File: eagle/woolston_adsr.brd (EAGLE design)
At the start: 100 x 80 mm, 39 parts, among them IC1 TL074P, Q1 2N3906, T1 2N3904

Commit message: almost layout
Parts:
- D2, D3: value 1N4148DO35-10 -> 1N4148DO35-7; device diode:DO35-10 -> diode:DO35-7
- moved R11 3.81 mm to (15.2, 22.9)
- moved R1 3.81 mm to (15.2, 19.1)
- moved R10 2.54 mm to (34.3, 20.3)
- moved R15 2.54 mm to (66.0, 22.9)
- moved D1 1.80 mm to (53.3, 11.4)
- moved D3 1.27 mm to (24.1, 15.2)
- moved R12 1.27 mm to (64.8, 14.0)
- moved R6 1.27 mm to (16.5, 41.9)
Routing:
- net N$4: track 69.7 -> 66.0 mm
- net GND: track 342.2 -> 339.4 mm
- net N$6: track 43.0 -> 45.8 mm
- net N$22: track 11.5 -> 14.1 mm
- net N$24: track 19.0 -> 16.7 mm
- net N$18: track 31.6 -> 33.5 mm
- net N$21: track 7.12 -> 5.24 mm
- net N$25: track 11.0 -> 9.20 mm
- net N$9: track 3.59 -> 4.58 mm
- net N$14: track 28.3 -> 29.3 mm
- net +12V: track 83.7 -> 84.6 mm

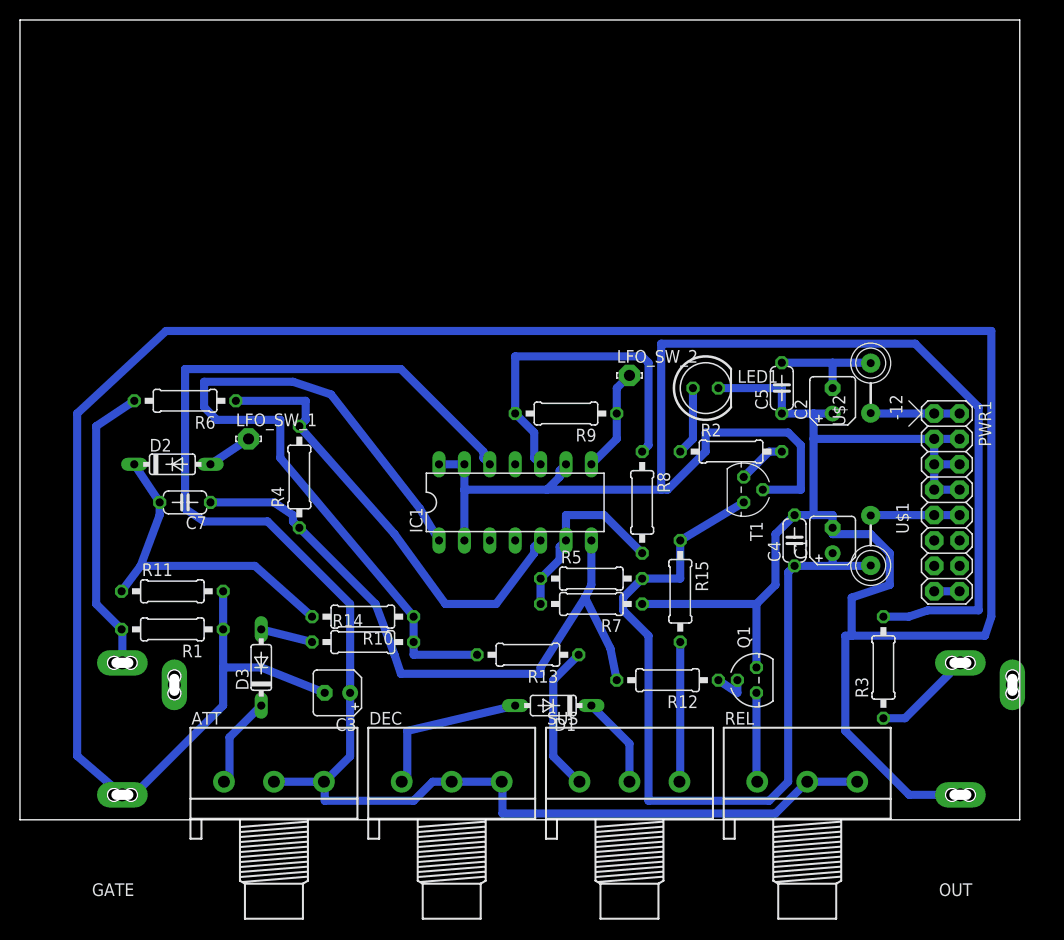
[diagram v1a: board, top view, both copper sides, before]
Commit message: fixed power to 074 and twiggled some
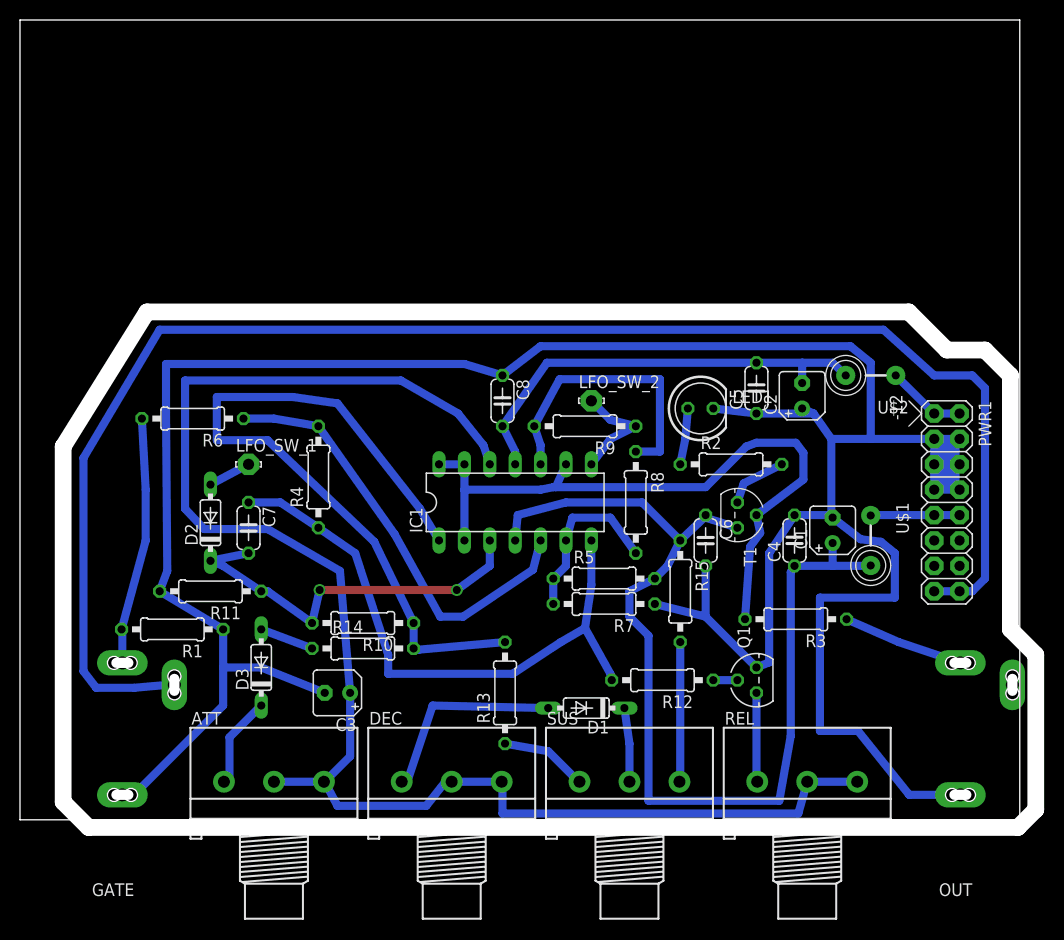
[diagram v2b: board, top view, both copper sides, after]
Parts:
- added C6, C8: 100n, rcl:C050-024X044
- moved R3 10.0 mm to (77.6, 20.1), turned to 180 degrees
- moved D2 6.97 mm to (19.1, 29.7), turned to 90 degrees
- moved C7 6.84 mm to (22.9, 29.2), turned to 270 degrees
- moved LFO_SW_2 4.58 mm to (57.1, 41.9)
- moved R13 4.44 mm to (48.5, 12.7), turned to 90 degrees
- moved R11 3.81 mm to (19.1, 22.9), turned to 180 degrees
- moved D1 3.31 mm to (56.6, 11.2)
- moved C2 3.09 mm to (78.2, 42.4)
- moved T1 2.62 mm to (71.8, 30.5)
- moved C5 2.54 mm to (73.7, 43.2)
- moved LFO_SW_1 2.54 mm to (22.9, 35.6)
- moved R9 2.29 mm to (56.5, 39.4)
- moved LED1 2.09 mm to (68.1, 41.1)
- moved R6 1.93 mm to (17.3, 40.1)
- moved R4 1.90 mm to (29.8, 34.3)
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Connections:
- removed net V+: IC1.4
- removed net V-: IC1.11
- net +12V: now also C6.1, IC1.4
- net -12V: now also C8.2, IC1.11
- net GND: now also C6.2, C8.1
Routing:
- net N$12: track 2.54 -> 155.7 mm
- net N$19: track 138.3 -> 68.2 mm
- net GND: track 339.4 -> 275.3 mm
- net -12V: track 11.5 -> 44.3 mm
- net +12V: track 84.6 -> 103.6 mm
- net N$18: track 33.5 -> 39.7 mm, vias 0 -> 2
- net N$16: track 14.9 -> 8.78 mm
- net N$10: track 34.6 -> 28.9 mm
- net N$4: track 66.0 -> 60.5 mm
- net N$14: track 29.3 -> 24.8 mm
- net N$24: track 16.7 -> 20.1 mm
- net N$20: track 76.5 -> 74.1 mm
- net N$15: track 9.99 -> 12.2 mm
- net N$6: track 45.8 -> 43.9 mm
- net N$25: track 9.20 -> 7.40 mm
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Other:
- board size 100 x 80 mm -> 101.6 x 80.8 mm

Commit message: verified and new panel
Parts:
- moved R7 2.79 mm to (58.4, 18.8)
- moved R5 2.54 mm to (58.4, 21.6)
- moved R15 2.29 mm to (66.0, 20.6)
- moved R12 1.30 mm to (64.0, 12.7)
- moved D1 0.76 mm to (56.6, 10.4)
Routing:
- net N$4: track 60.5 -> 64.6 mm
- net N$7: track 17.4 -> 20.2 mm
- net N$24: track 20.1 -> 17.5 mm
- net GND: track 275.3 -> 272.7 mm
- net N$22: track 14.1 -> 11.8 mm
- net N$25: track 7.40 -> 6.65 mm
- net +12V: track 103.6 -> 104.3 mm
- net N$18: track 39.7 -> 40.3 mm
- net N$6: track 43.9 -> 44.5 mm
- net N$11: track 2.41 -> 2.95 mm
